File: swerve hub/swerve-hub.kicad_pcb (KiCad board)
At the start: 2 copper layers, 32.5 x 50.3 mm, 5 parts, among them J1 RJ45_LED_Shielded, J2 Conn_01x02_Pin, J3 Conn_01x02_Pin, J4 Conn_01x03_Pin

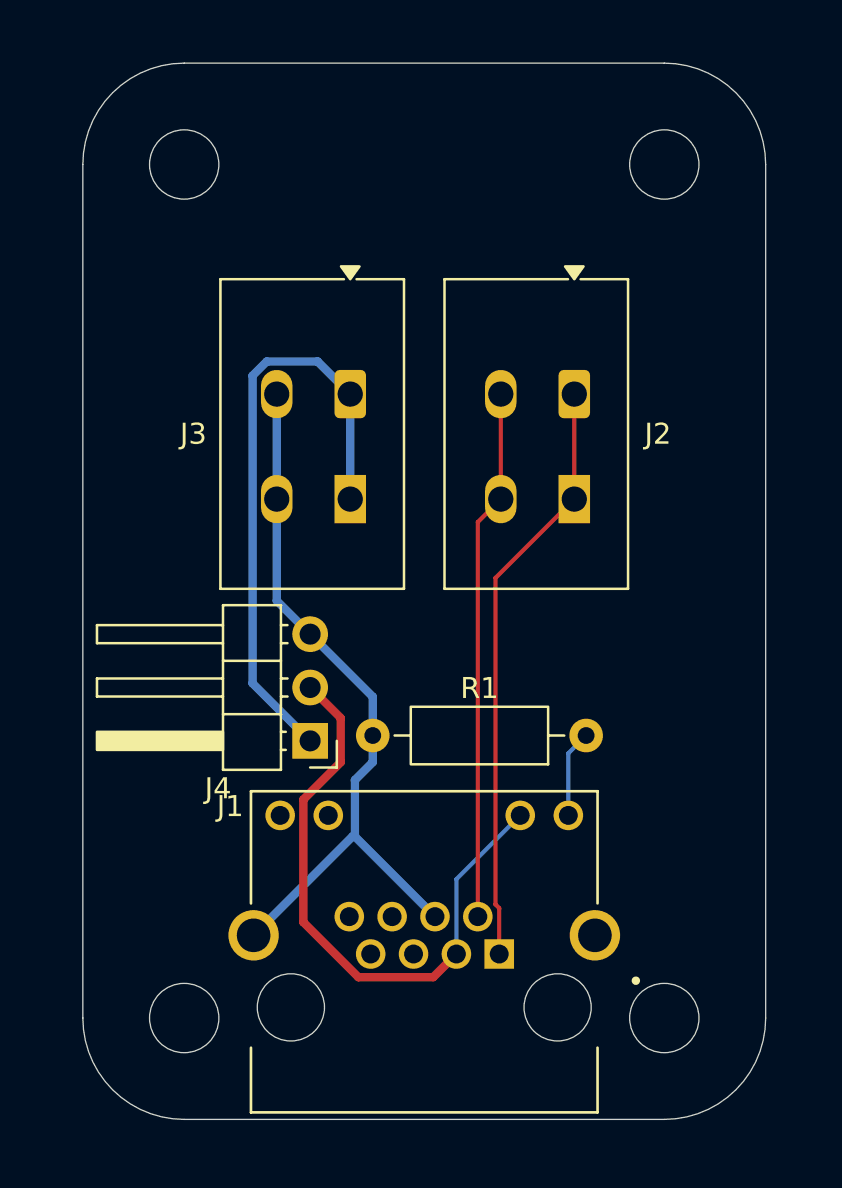
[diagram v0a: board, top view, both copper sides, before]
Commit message: swerve hub pcb rearrange and added reverse polarity protection
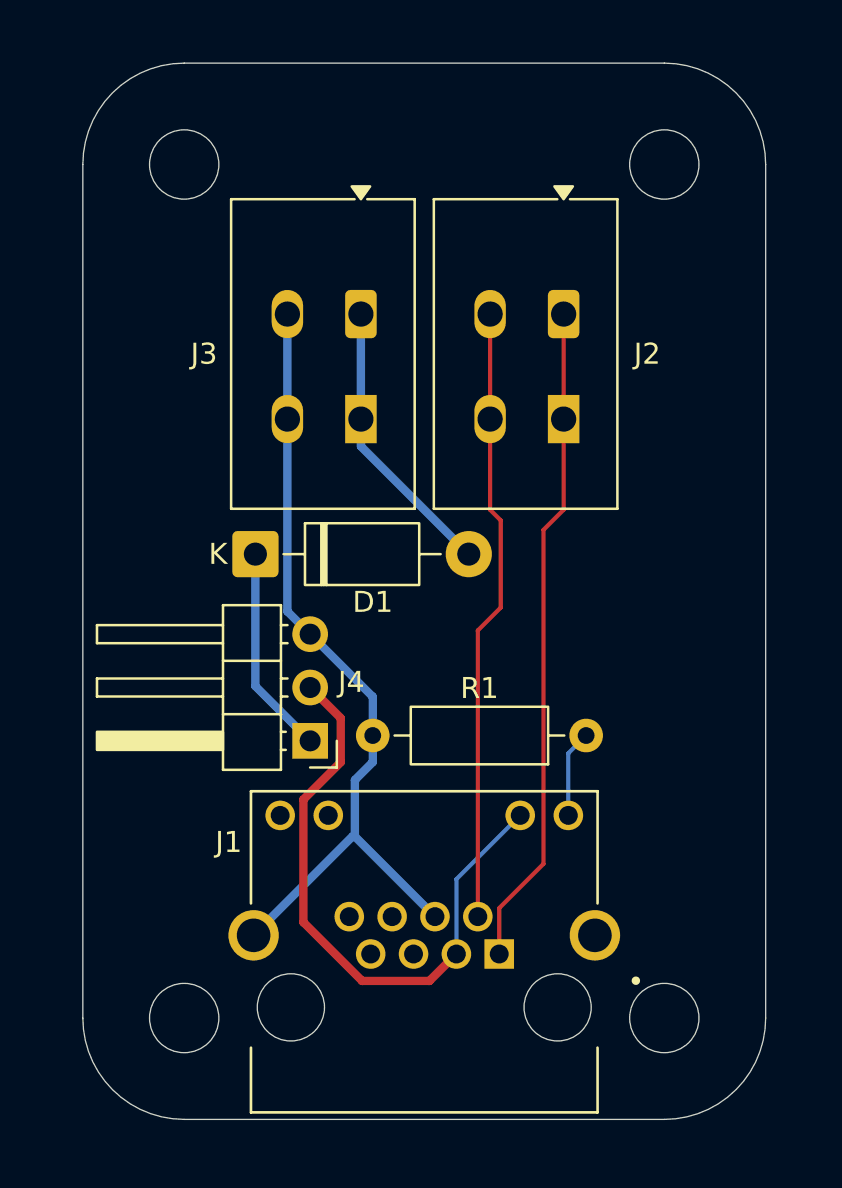
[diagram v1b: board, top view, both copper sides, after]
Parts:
- added D1: D_Schottky, Diode_THT:D_DO-41_SOD81_P10.16mm_Horizontal, F.Cu at (89.9, 82.8)
- moved J2 3.84 mm to (104.6, 71.4)
- moved J3 3.84 mm to (94.9, 71.4)
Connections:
- J4 pad 1: /12v -> Net-(D1-K)
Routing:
- net /12v: track 29.1 -> 13.6 mm
- net Net-(D1-K): track 0.00 -> 9.97 mm
- net /CANl: track 25.3 -> 29.4 mm
- net /GND: track 35.6 -> 39.1 mm
- net /CANh: track 28.3 -> 31.7 mm

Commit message: swerve can improvements, ground planes, removed excess wagos
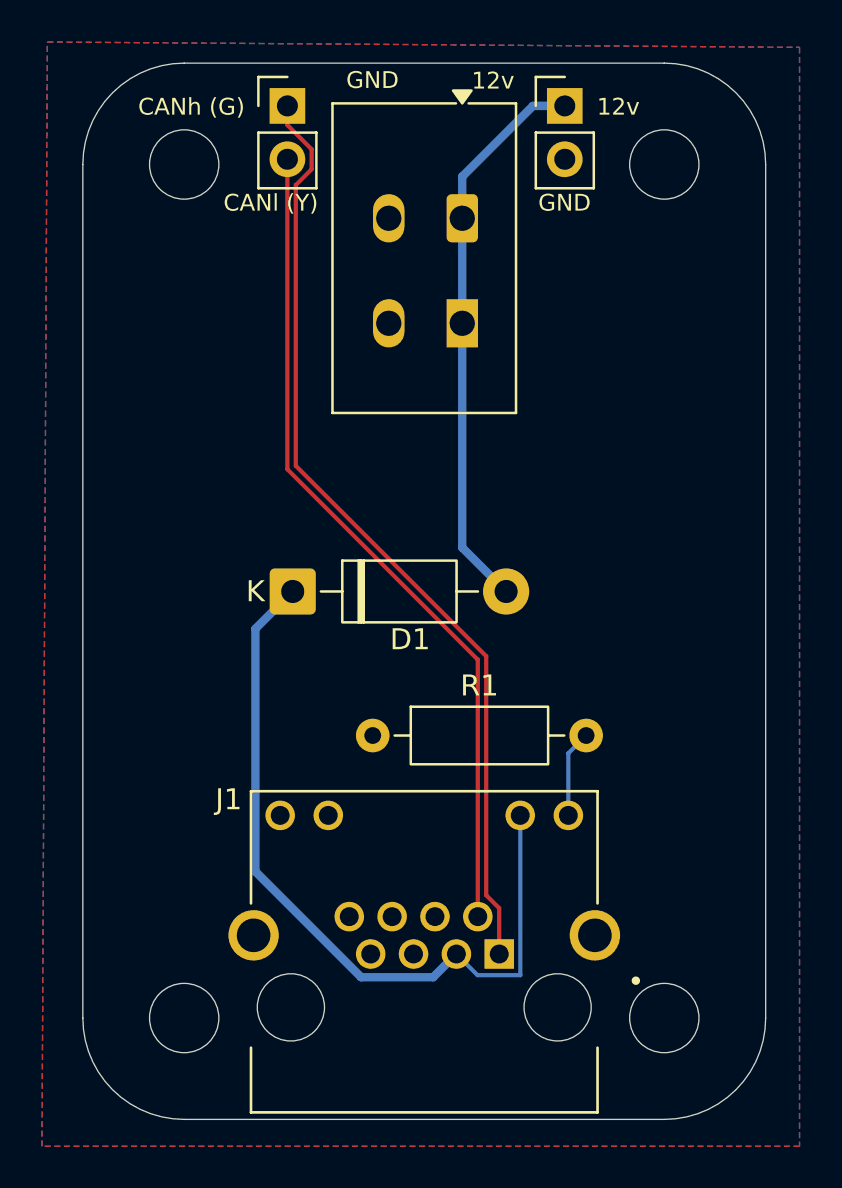
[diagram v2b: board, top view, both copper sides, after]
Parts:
- J1: value RJ45_LED_Shielded -> MTJ-88ARX1-FSM-LG
- J2: footprint TerminalBlock_WAGO:TerminalBlock_WAGO_2601-1102_1x02_P3.50mm_Horizontal -> Connector_PinHeader_2.54mm:PinHeader_1x02_P2.54mm_Vertical
- J4: value Conn_01x03_Pin -> Conn_01x02_Pin; footprint Connector_PinHeader_2.54mm:PinHeader_1x03_P2.54mm_Horizontal -> Connector_PinHeader_2.54mm:PinHeader_1x02_P2.54mm_Vertical
- moved J4 32.6 mm to (104.6, 61.5), turned to 0 degrees
- moved J2 16.5 mm to (91.4, 61.5), turned to 0 degrees
- moved R1 10.2 mm to (95.5, 91.4), turned to 0 degrees
- moved J3 6.64 mm to (99.8, 66.8)
- moved D1 2.51 mm to (91.7, 84.6)
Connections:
- J1 pad 10: Net-(J4-Pin_2) -> Net-(D1-K)
- J1 pad 3: Net-(J4-Pin_2) -> Net-(D1-K)
- J1 pad SH2: (no net) -> /GND
- J4 pad 1: Net-(D1-K) -> /12v
- J4 pad 2: Net-(J4-Pin_2) -> /GND
- R1 pad 1: Net-(J1-Pad9) -> /GND
- R1 pad 2: /GND -> Net-(J1-Pad9)
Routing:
- net /GND: track 39.1 -> 0.00 mm
- net Net-(J4-Pin_2): track 29.3 -> 0.00 mm
- net Net-(D1-K): track 9.97 -> 37.3 mm
- net /CANh: track 31.7 -> 45.2 mm
- net /12v: track 13.6 -> 26.9 mm
- net /CANl: track 29.4 -> 39.8 mm
- added copper zone on B.Cu, net /GND
- added copper zone on F.Cu, net /GND
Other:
- board text added: "12v"
- board text added: "CANh (G)"
- board text added: "CANl (Y)"
- board text added: "GND"

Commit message: fixed diode placement, major rio hub work
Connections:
- D1 pad 1: Net-(D1-K) -> /12v
- D1 pad 2: /12v -> Net-(D1-A)
- J1 pad 10: Net-(D1-K) -> /12v
- J1 pad 3: Net-(D1-K) -> /12v
- J3 pad 1: /12v -> Net-(D1-A)
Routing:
- net /12v: track 26.9 -> 70.3 mm
- net Net-(D1-K): track 37.3 -> 0.00 mm
- net Net-(D1-A): track 0.00 -> 18.6 mm
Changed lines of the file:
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@@
 	(net 10 "/12v")
 	(net 11 "Net-(J1-Pad9)")
-	(net 12 "Net-(D1-K)")
+	(net 12 "Net-(D1-A)")
 	(footprint "TerminalBlock_WAGO:TerminalBlock_WAGO_2601-1102_1x02_P3.50mm_Horizontal"
 		(layer "F.Cu")
@@
 			(layers "*.Cu" "*.Mask")
 			(remove_unused_layers no)
-			(net 10 "/12v")
+			(net 12 "Net-(D1-A)")
 			(pinfunction "Pin_1")
 			(pintype "passive")
@@
 			(remove_unused_layers no)
 			(roundrect_rratio 0.166667)
-			(net 10 "/12v")
+			(net 12 "Net-(D1-A)")
 			(pinfunction "Pin_1")
 			(pintype "passive")
@@
 			(layers "*.Cu" "*.Mask")
 			(remove_unused_layers no)
-			(net 12 "Net-(D1-K)")
+			(net 10 "/12v")
 			(pinfunction "3")
 			(pintype "passive")
@@
 			(layers "*.Cu" "*.Mask")
 			(remove_unused_layers no)
-			(net 12 "Net-(D1-K)")
+			(net 10 "/12v")
 			(pintype "passive")
 			(solder_mask_margin 0.102)
@@
 			(remove_unused_layers no)
 			(roundrect_rratio 0.113636)
-			(net 12 "Net-(D1-K)")
+			(net 10 "/12v")
 			(pinfunction "K")
 			(pintype "passive")
@@
 			(layers "*.Cu" "*.Mask")
 			(remove_unused_layers no)
-			(net 10 "/12v")
+			(net 12 "Net-(D1-A)")
 			(pinfunction "A")
 			(pintype "passive")
@@
 	)
 	(segment
-		(start 99.766 71.8125)
-		(end 99.766 82.494)
+		(start 91.694 84.582)
+		(end 89.916 86.36)
 		(width 0.4)
 		(layer "B.Cu")
@@
 	)
 	(segment
-		(start 99.766 64.826)
-		(end 103.129 61.463)
+		(start 89.916 86.36)
+		(end 89.916 97.916206)
 		(width 0.4)
 		(layer "B.Cu")
@@
 	)
 	(segment
-		(start 99.766 66.8125)
-		(end 99.766 64.826)
+		(start 102.531 102.8485)
+		(end 100.491 102.8485)
+		(width 0.2)
+		(layer "B.Cu")
+		(net 10)
+	)
+	(segment
+		(start 94.25 64)
+		(end 94.25 78)
+		(width 0.2)
+		(layer "B.Cu")
+		(net 10)
+	)
+	(segment
+		(start 96.787 61.463)
+		(end 94.25 64)
+		(width 0.2)
+		(layer "B.Cu")
+		(net 10)
+	)
+	(segment
+		(start 94.948294 102.9485)
+		(end 98.381 102.9485)
 		(width 0.4)
 		(layer "B.Cu")
 		(net 10)
+	)
+	(segment
+		(start 98.381 102.9485)
+		(end 99.486 101.8435)
+		(width 0.4)
+		(layer "B.Cu")
+		(net 10)
+	)
+	(segment
+		(start 91.694 80.556)
+		(end 91.694 84.582)
+		(width 0.2)
+		(layer "B.Cu")
+		(net 10)
+	)
+	(segment
+		(start 104.648 61.463)
+		(end 96.787 61.463)
+		(width 0.2)
+		(layer "B.Cu")
+		(net 10)
+	)
+	(segment
+		(start 94.25 78)
+		(end 91.694 80.556)
+		(width 0.2)
+		(layer "B.Cu")
+		(net 10)
+	)
+	(segment
+		(start 89.916 97.916206)
+		(end 94.948294 102.9485)
+		(width 0.4)
+		(layer "B.Cu")
+		(net 10)
+	)
+	(segment
+		(start 100.491 102.8485)
+		(end 99.486 101.8435)
+		(width 0.2)
+		(layer "B.Cu")
+		(net 10)
+	)
+	(segment
+		(start 102.531 95.2485)
+		(end 102.531 102.8485)
+		(width 0.2)
+		(layer "B.Cu")
+		(net 10)
+	)
+	(segment
+		(start 102.526 95.2435)
+		(end 102.531 95.2485)
+		(width 0.2)
+		(layer "B.Cu")
+		(net 10)
+	)
+	(segment
+		(start 104.816 95.2435)
+		(end 104.816 92.288)
+		(width 0.2)
+		(layer "B.Cu")
+		(net 11)
+	)
+	(segment
+		(start 104.816 92.288)
+		(end 105.664 91.44)
+		(width 0.2)
+		(layer "B.Cu")
+		(net 11)
+	)
+	(segment
+		(start 101.854 84.582)
+		(end 99.75 82.478)
+		(width 0.4)
+		(layer "B.Cu")
+		(net 12)
 	)
 	(segment
@@
 		(width 0.4)
 		(layer "B.Cu")
-		(net 10)
-	)
-	(segment
-		(start 99.766 82.494)
-		(end 101.854 84.582)
-		(width 0.4)
-		(layer "B.Cu")
-		(net 10)
-	)
-	(segment
-		(start 103.129 61.463)
-		(end 104.648 61.463)
-		(width 0.4)
-		(layer "B.Cu")
-		(net 10)
-	)
-	(segment
-		(start 104.816 95.2435)
-		(end 104.816 92.288)
-		(width 0.2)
-		(layer "B.Cu")
-		(net 11)
-	)
-	(segment
-		(start 104.816 92.288)
-		(end 105.664 91.44)
-		(width 0.2)
-		(layer "B.Cu")
-		(net 11)
-	)
-	(segment
-		(start 91.694 84.582)
-		(end 89.916 86.36)
+		(net 12)
+	)
+	(segment
+		(start 99.766 82.462)
+		(end 99.766 71.8125)
 		(width 0.4)
 		(layer "B.Cu")
@@
 	)
 	(segment
-		(start 89.916 86.36)
-		(end 89.916 97.916206)
+		(start 99.75 82.478)
+		(end 99.766 82.462)
 		(width 0.4)
 		(layer "B.Cu")
 		(net 12)
-	)
-	(segment
-		(start 102.531 102.8485)
-		(end 100.491 102.8485)
-		(width 0.2)
-		(layer "B.Cu")
-		(net 12)
-	)
-	(segment
-		(start 94.948294 102.9485)
-		(end 98.381 102.9485)
-		(width 0.4)
-		(layer "B.Cu")
-		(net 12)
-	)
-	(segment
-		(start 98.381 102.9485)
-		(end 99.486 101.8435)
-		(width 0.4)
-		(layer "B.Cu")
-		(net 12)
-	)
-	(segment
-		(start 89.916 97.916206)
-		(end 94.948294 102.9485)
-		(width 0.4)
-		(layer "B.Cu")
-		(net 12)
-	)
-	(segment
-		(start 100.491 102.8485)
-		(end 99.486 101.8435)
-		(width 0.2)
-		(layer "B.Cu")
-		(net 12)
-	)
-	(segment
-		(start 102.531 95.2485)
-		(end 102.531 102.8485)
-		(width 0.2)
-		(layer "B.Cu")
-		(net 12)
-	)
-	(segment
-		(start 102.526 95.2435)
-		(end 102.531 95.2485)
-		(width 0.2)
-		(layer "B.Cu")
-		(net 12)

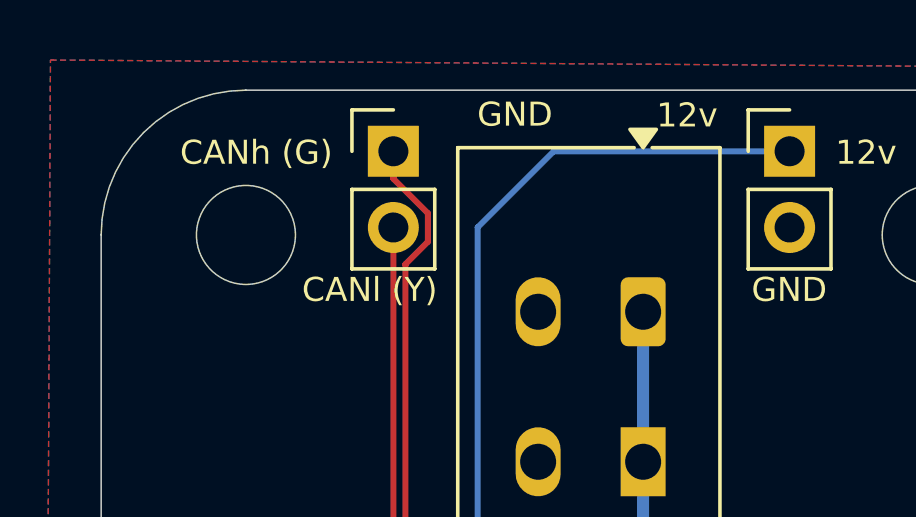
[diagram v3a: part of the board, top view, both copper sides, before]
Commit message: rio module and added better silkscreening
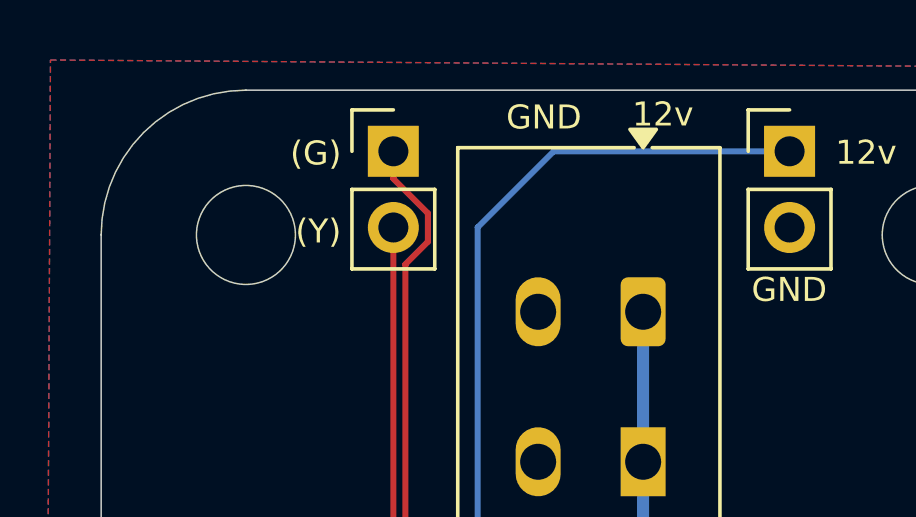
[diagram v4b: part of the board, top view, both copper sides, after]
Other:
- board text added: "(G)"
- board text added: "(Y)"
- board text removed: "CANh (G)"
- board text removed: "CANl (Y)"
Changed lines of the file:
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@@
 		(layer "Edge.Cuts")
 	)
-	(gr_text "CANh (G)"
-		(at 84.328 61.976 0)
+	(gr_text "(G)"
+		(at 88 62 0)
 		(layer "F.SilkS")
 		(effects
@@
 	)
 	(gr_text "GND"
-		(at 94.234 60.706 0)
+		(at 95.2 60.8 0)
 		(layer "F.SilkS")
 		(effects
@@
 	)
 	(gr_text "12v\n"
-		(at 100.206 60.7325 0)
+		(at 99.4 60.7 0)
 		(layer "F.SilkS")
 		(effects
@@
 		)
 	)
-	(gr_text "CANl (Y)"
-		(at 88.392 66.548 0)
+	(gr_text "(Y)"
+		(at 88.176 64.6 0)
 		(layer "F.SilkS")
 		(effects

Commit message: final major changes, exported for JLCPCB
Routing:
- net /12v: track 70.3 -> 70.9 mm
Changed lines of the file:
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@@
 		(tenting front back)
 		(pcbplotparams
-			(layerselection 0x00000000_00000000_55555555_5755f5ff)
+			(layerselection 0x00000000_00000000_55555555_575555ff)
 			(plot_on_all_layers_selection 0x00000000_00000000_00000000_00000000)
 			(disableapertmacros no)
-			(usegerberextensions no)
+			(usegerberextensions yes)
 			(usegerberattributes yes)
 			(usegerberadvancedattributes yes)
@@
 			(plotframeref no)
 			(mode 1)
-			(useauxorigin no)
+			(useauxorigin yes)
 			(hpglpennumber 1)
 			(hpglpenspeed 20)
@@
 			(plotpadnumbers no)
 			(hidednponfab no)
-			(sketchdnponfab yes)
-			(crossoutdnponfab yes)
+			(sketchdnponfab no)
+			(crossoutdnponfab no)
 			(subtractmaskfromsilk no)
 			(outputformat 1)
 			(mirror no)
-			(drillshape 1)
+			(drillshape 0)
 			(scaleselection 1)
-			(outputdirectory "")
+			(outputdirectory "JLC/")
 		)
 	)
@@
 	)
 	(segment
-		(start 102.531 102.8485)
-		(end 100.491 102.8485)
-		(width 0.2)
+		(start 102.526 95.2435)
+		(end 102.75 95.4675)
+		(width 0.4)
 		(layer "B.Cu")
 		(net 10)
@@
 		(start 94.25 64)
 		(end 94.25 78)
-		(width 0.2)
+		(width 0.4)
 		(layer "B.Cu")
 		(net 10)
@@
 		(start 96.787 61.463)
 		(end 94.25 64)
-		(width 0.2)
+		(width 0.4)
 		(layer "B.Cu")
 		(net 10)
@@
 	)
 	(segment
+		(start 102.75 103)
+		(end 100.6425 103)
+		(width 0.4)
+		(layer "B.Cu")
+		(net 10)
+	)
+	(segment
 		(start 98.381 102.9485)
 		(end 99.486 101.8435)
@@
 		(start 91.694 80.556)
 		(end 91.694 84.582)
-		(width 0.2)
+		(width 0.4)
 		(layer "B.Cu")
 		(net 10)
@@
 		(start 104.648 61.463)
 		(end 96.787 61.463)
-		(width 0.2)
+		(width 0.4)
 		(layer "B.Cu")
 		(net 10)
 	)
 	(segment
+		(start 102.75 95.4675)
+		(end 102.75 103)
+		(width 0.4)
+		(layer "B.Cu")
+		(net 10)
+	)
+	(segment
 		(start 94.25 78)
 		(end 91.694 80.556)
-		(width 0.2)
+		(width 0.4)
 		(layer "B.Cu")
 		(net 10)
@@
 	)
 	(segment
-		(start 100.491 102.8485)
+		(start 100.6425 103)
 		(end 99.486 101.8435)
-		(width 0.2)
+		(width 0.4)
 		(layer "B.Cu")
 		(net 10)
-	)
-	(segment
-		(start 102.531 95.2485)
-		(end 102.531 102.8485)
-		(width 0.2)
-		(layer "B.Cu")
-		(net 10)
-	)
-	(segment
-		(start 102.526 95.2435)
-		(end 102.531 95.2485)
-		(width 0.2)
-		(layer "B.Cu")
-		(net 10)
